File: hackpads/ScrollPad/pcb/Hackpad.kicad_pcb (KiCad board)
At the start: 2 copper layers, 61.9 x 61.9 mm, 10 parts, among them SW1 SW_Push, SW2 SW_Push, SW3 SW_Push, SW4 SW_Push, SW5 SW_Push, U1 XIAO-RP2040-DIP

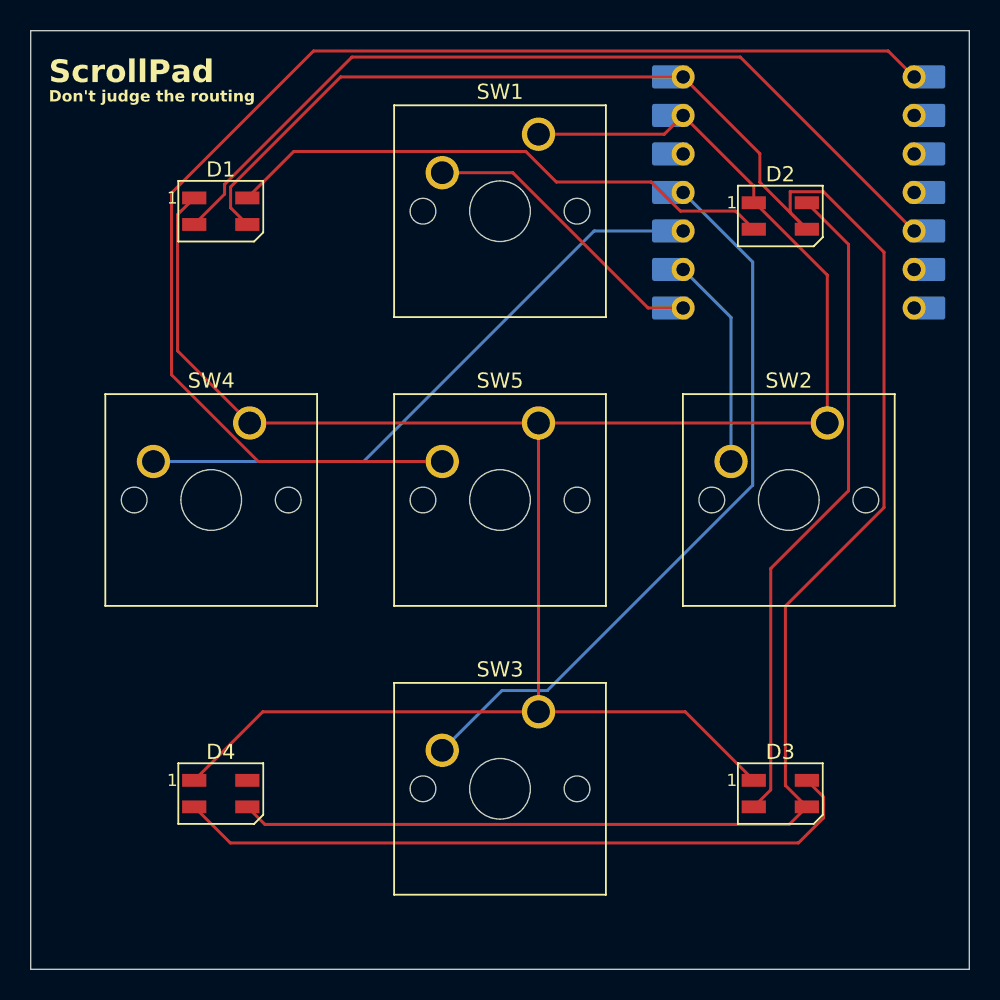
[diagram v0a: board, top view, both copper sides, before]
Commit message: Update ScrollPad hardware and firmware
- Change GPIO pin assignments
- PCB improvements: add mounting holes, LED position, routing
- Case improvements: add spacer, cover fix, add Skadis holder
- Update firmware: add LED layer indication, add mouse scrolling keys, change keys
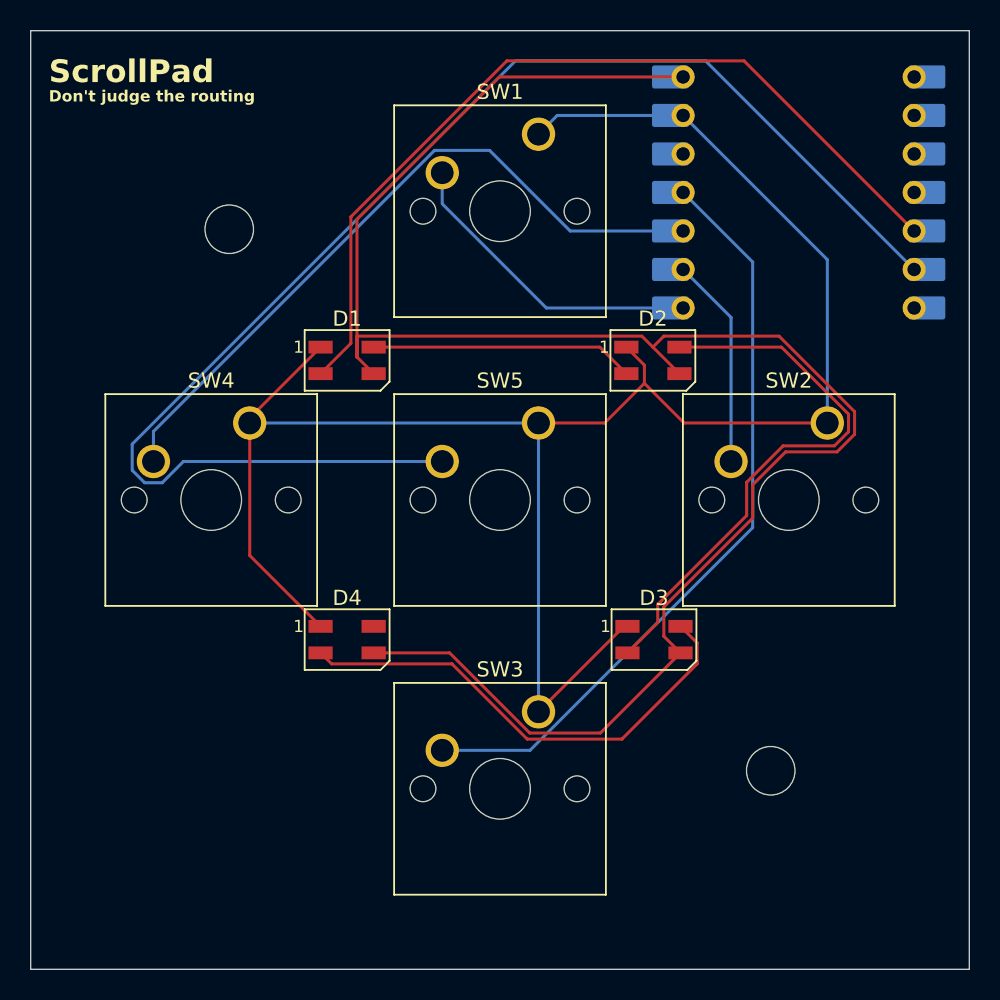
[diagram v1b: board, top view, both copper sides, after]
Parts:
- added REF**: MountingHole_3.2mm_M3, MountingHole:MountingHole_3.2mm_M3, F.Cu at (98.8, 89.3)
- added REF**: MountingHole_3.2mm_M3, MountingHole:MountingHole_3.2mm_M3, F.Cu at (134.5, 125.0)
- moved D3 13.1 mm to (126.8, 116.4)
- moved D4 13.1 mm to (106.6, 116.4)
- moved D1 12.9 mm to (106.6, 97.9)
- moved D2 12.7 mm to (126.8, 97.9)
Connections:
- SW5 pad 2: Net-(U1-GPIO26/ADC0/A0) -> Net-(U1-GPIO7/SCL)
- U1 pad 1: Net-(U1-GPIO26/ADC0/A0) -> unconnected-(U1-GPIO26/ADC0/A0-Pad1)
- U1 pad 6: unconnected-(U1-GPIO7/SCL-Pad6) -> Net-(U1-GPIO7/SCL)
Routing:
- net Net-(U1-GPIO7/SCL): track 0.00 -> 90.8 mm
- net Net-(U1-GPIO26/ADC0/A0): track 85.8 -> 0.00 mm
- net GND: track 149.4 -> 127.0 mm
- net Net-(D1-DOUT): track 36.8 -> 17.4 mm
- net +5V: track 137.7 -> 123.6 mm
- net Net-(D3-DOUT): track 46.1 -> 32.2 mm
- net Net-(D2-DOUT): track 43.6 -> 36.8 mm
- net Net-(U1-GPIO4/MISO): track 41.2 -> 46.8 mm
- net Net-(U1-GPIO3/MOSI): track 48.9 -> 50.6 mm
- net Net-(U1-GPIO1/RX): track 19.6 -> 20.8 mm
